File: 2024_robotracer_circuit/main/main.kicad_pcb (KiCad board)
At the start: 2 copper layers, 60 x 60 mm, 93 parts, among them J1 PH_6p, J10 PH_5p, J11 PH_6p, J12 PH_4p, J13 PH_8p, J14 PH_6p, J2 Conn_02x05_Odd_Even, J3 Conn_02x05_Odd_Even, J4 PA_2p, J5 PA_2p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

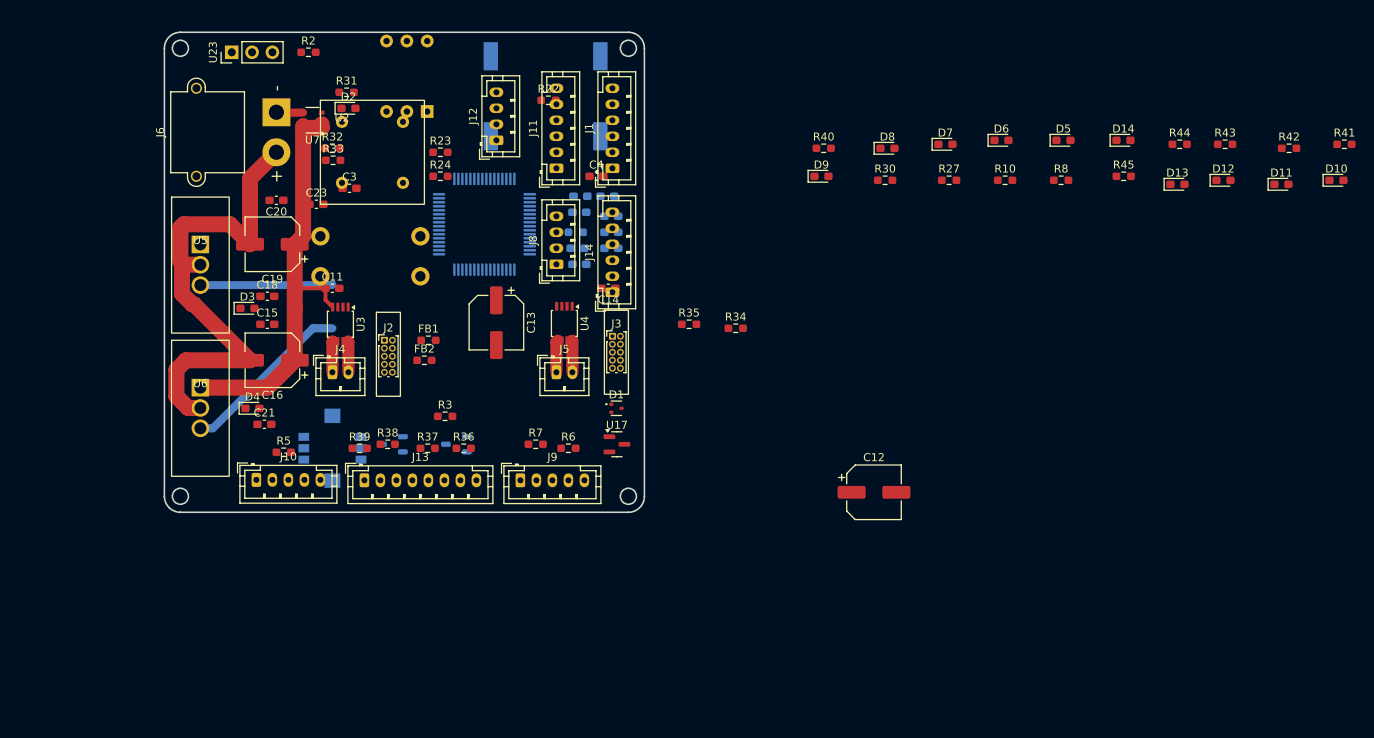
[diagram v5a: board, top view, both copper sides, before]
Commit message: LED基板分けた
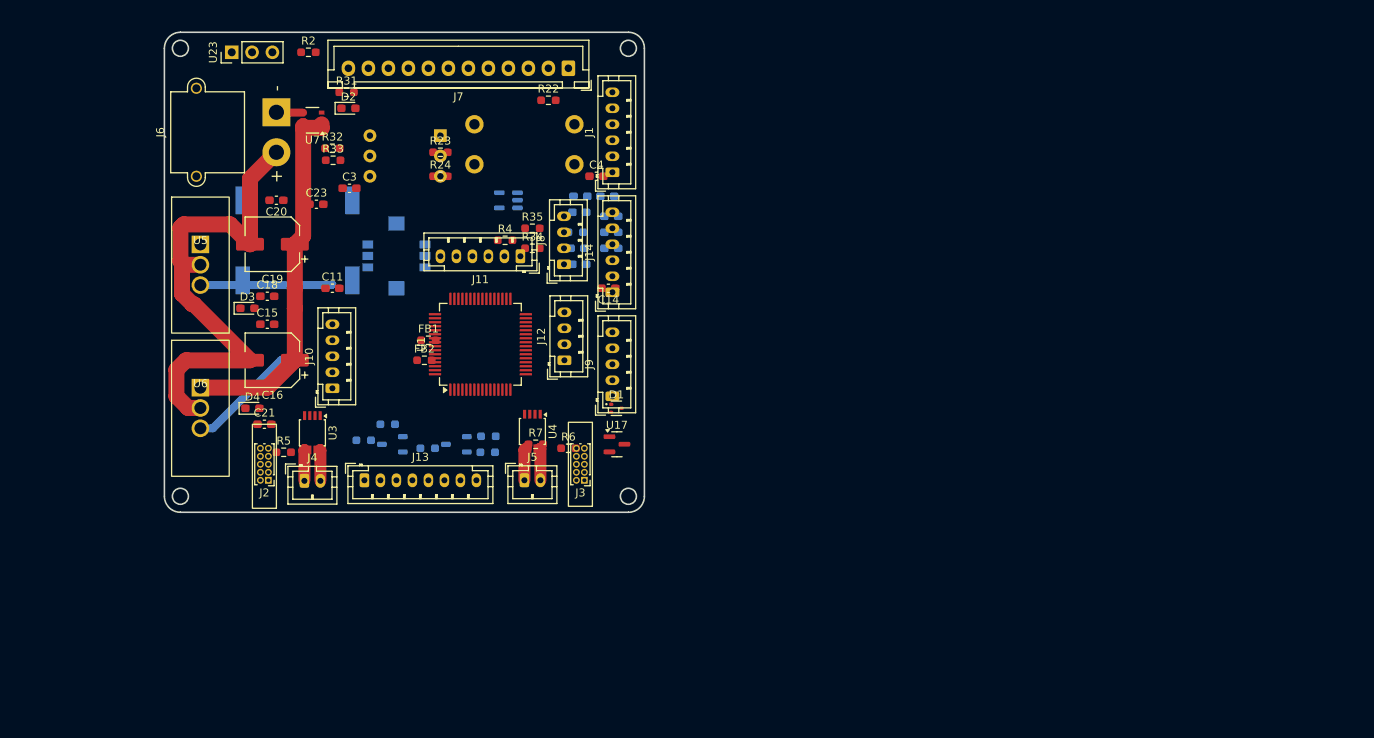
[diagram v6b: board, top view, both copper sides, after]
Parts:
- removed C12, C13: 100u, Capacitor_SMD:CP_Elec_6.3x5.4
- removed D10, D11, D12, D13, D14, D5, D6, D7, D8, D9: LED_Small, LED_SMD:LED_0603_1608Metric_Pad1.05x0.95mm_HandSolder
- removed R10, R27, R30, R40, R41, R42, R43, R44, R45, R8: R_Small, Resistor_SMD:R_0603_1608Metric_Pad0.98x0.95mm_HandSolder
- added J7: HX_12p, Connector_JST:JST_XH_B12B-XH-A_1x12_P2.50mm_Vertical, F.Cu at (148.5, 42.5)
- added R4: 1k, Resistor_SMD:R_0603_1608Metric_Pad0.98x0.95mm_HandSolder, F.Cu at (140.6, 64.0)
- R3, R36, R37, R38, R39: moved to B.Cu
- U1: moved to F.Cu
- U2: value OSC8MI/H -> SIT2001B; footprint mylib:OSC8MIH -> Package_TO_SOT_SMD:TSOT-23-5; moved to B.Cu
- moved BZ1 52.7 mm to (107.8, 69.0), turned to 0 degrees
- moved J12 28.8 mm to (148.0, 79.0)
- moved R34 27.3 mm to (144.0, 65.0)
- moved U22 25.3 mm to (127.0, 66.0)
- moved SW1 23.8 mm to (149.2, 49.5)
- moved U2 23.0 mm to (141.0, 59.0), turned to 180 degrees
- moved R35 23.0 mm to (144.0, 62.5)
- moved J2 22.7 mm to (111.0, 94.0), turned to 180 degrees
- moved J3 18.3 mm to (150.5, 94.0), turned to 180 degrees
- moved J9 15.6 mm to (154.0, 83.5), turned to 90 degrees
- moved U1 15.0 mm to (137.5, 77.0), turned to 90 degrees
- moved J10 14.9 mm to (119.0, 82.5), turned to 90 degrees
- moved J5 14.1 mm to (143.0, 94.0)
- moved U4 14.1 mm to (144.0, 87.9)
- moved J4 14.0 mm to (115.5, 94.1)
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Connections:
- U2 pad 1: unconnected-(U2-NC-Pad1) -> GND
- U2 pad 4: GND -> +3.3V
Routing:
- net +5V: track 21.7 -> 15.0 mm
- net +BATT: track 52.4 -> 45.9 mm

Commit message: 配線途中
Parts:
- C1, C10, C5, C6, C7, C8, C9, R1: moved to F.Cu
- R2, R4: moved to B.Cu
- moved U2 26.3 mm to (130.4, 83.1), turned to -90 degrees
- moved C21 22.5 mm to (120.0, 66.6)
- moved C1 22.4 mm to (129.1, 66.4), turned to 0 degrees
- moved D4 22.1 mm to (120.3, 66.0)
- moved R4 20.9 mm to (133.8, 83.8), turned to 180 degrees
- moved R31 18.2 mm to (119.3, 63.6)
- moved C2 17.9 mm to (143.2, 73.2)
- moved C9 17.1 mm to (136.7, 65.4), turned to 0 degrees
- moved U22 16.6 mm to (119.8, 51.0)
- moved D2 14.2 mm to (119.2, 61.6)
- moved C7 14.0 mm to (141.8, 68.2), turned to 0 degrees
- moved C6 13.4 mm to (140.8, 66.0), turned to 0 degrees
- moved D3 13.1 mm to (119.4, 65.4)
- moved R2 12.6 mm to (105.5, 47.5), turned to 90 degrees
- moved R32 12.3 mm to (121.2, 64.6)
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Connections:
- J11 pad 2: /SDIO_CMD -> /SDIO_D0
- J11 pad 3: /SDIO_CK -> /SDIO_SW
- J11 pad 4: /SDIO_D0 -> /SDIO_CK
- J11 pad 5: /SDIO_SW -> /SDIO_CMD
- J8 pad 2: /LCD_SDA -> /LCD_SCL
- J8 pad 3: /LCD_SCL -> /LCD_SDA
- R34 pad 2: /LCD_SDA -> /LCD_SCL
- R35 pad 2: /LCD_SCL -> /LCD_SDA
- U1 pad 37: /ENC2_A -> /ENC2_B
- U1 pad 38: /ENC2_B -> /ENC2_A
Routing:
- net GND: track 62.4 -> 238.4 mm
- net +3.3V: track 16.5 -> 79.2 mm
- net /SWO: track 0.00 -> 45.3 mm, vias 0 -> 1
- net +5V: track 15.0 -> 60.3 mm
- net +BATT: track 45.9 -> 86.1 mm
- net /SWDIO: track 0.00 -> 37.6 mm, vias 0 -> 1
- net /SWCLK: track 0.00 -> 34.2 mm, vias 0 -> 1
- net /ENC1_A: track 0.00 -> 32.2 mm, vias 0 -> 2
- net /MOTOR1_IN_A: track 0.00 -> 31.1 mm, vias 0 -> 2
- net /MOTOR1_IN_B: track 0.00 -> 30.8 mm, vias 0 -> 2
- net /ENC2_A: track 0.00 -> 30.1 mm, vias 0 -> 1
- net /ENC1_B: track 0.00 -> 29.4 mm, vias 0 -> 2
- net /ENC2_B: track 0.00 -> 28.5 mm, vias 0 -> 1
- net /MOTOR2_IN_A: track 0.00 -> 24.8 mm, vias 0 -> 2
- net /MOTOR2_IN_B: track 0.00 -> 24.5 mm, vias 0 -> 2
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
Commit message: マイコン向き変えたい
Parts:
- removed C10: 0.1u, Capacitor_SMD:C_0603_1608Metric_Pad1.08x0.95mm_HandSolder
- removed FB1, FB2: FerriteBead_Small, Resistor_SMD:R_0603_1608Metric_Pad0.98x0.95mm_HandSolder
- C4, R5, R7: moved to B.Cu
- moved C4 37.4 mm to (127.0, 83.8), turned to -90 degrees
- moved R7 21.3 mm to (123.3, 86.8), turned to 180 degrees
- moved R5 19.0 mm to (121.6, 73.6), turned to -90 degrees
- moved C14 17.8 mm to (141.8, 83.4)
- moved R1 17.4 mm to (125.8, 77.4), turned to -90 degrees
- moved R36 11.4 mm to (127.0, 89.6), turned to -90 degrees
- moved R39 10.1 mm to (133.0, 89.7), turned to -90 degrees
- moved C6 9.69 mm to (142.1, 75.6)
- moved C8 7.47 mm to (142.6, 70.4)
- moved R38 5.71 mm to (131.0, 89.6), turned to -90 degrees
- moved R4 5.20 mm to (128.6, 83.8), turned to -90 degrees
- moved U10 3.59 mm to (122.9, 89.5)
- moved R37 1.95 mm to (129.0, 89.6), turned to -90 degrees
- moved U8 1.80 mm to (136.3, 89.7)
- moved R3 1.78 mm to (139.8, 89.7), turned to -90 degrees
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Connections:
- J12 pad 2: /USART_TX -> /USART_RX
- J12 pad 3: /USART_RX -> /USART_TX
- U1 pad 12: GNDA -> GND
- U1 pad 13: VDDA -> +3.3V
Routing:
- net +3.3V: track 79.2 -> 239.5 mm
- net GND: track 238.4 -> 321.9 mm, vias 0 -> 2
- net Net-(J10-Pin_4): track 0.00 -> 60.1 mm, vias 0 -> 3
- net /SENSOR_PWM: track 0.00 -> 41.7 mm, vias 0 -> 3
- net /SENSOR_L_ADC: track 0.00 -> 32.7 mm, vias 0 -> 2
- net /SPI_MOSI_GP: track 0.00 -> 30.5 mm
- net /SPI_MISO_GP: track 0.00 -> 30.2 mm
- net /USART_RX: track 0.00 -> 26.3 mm, vias 0 -> 1
- net /USART_TX: track 0.00 -> 24.1 mm, vias 0 -> 1
- net /PWM_GP: track 0.00 -> 21.2 mm, vias 0 -> 1
- net +5V: track 60.3 -> 81.1 mm
- net /SENSOR0_ADC: track 0.00 -> 20.7 mm, vias 0 -> 1
- net /SENSOR1_ADC: track 0.00 -> 20.0 mm, vias 0 -> 1
- net /SENSOR2_ADC: track 0.00 -> 19.5 mm, vias 0 -> 1
- net /SPI_SCK_GP: track 0.00 -> 19.3 mm, vias 0 -> 1
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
